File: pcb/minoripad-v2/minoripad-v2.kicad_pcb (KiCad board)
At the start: 2 copper layers, 70 x 50 mm, 42 parts, among them J1 USB_C_Receptacle_USB2.0, SW1 SW_Push, SW2 SW_Push, U1 W25Q16JVSSIQ, U2 SRV05-4, U3 XC6206P332MR, U4 RP2040, Y1 12MHz

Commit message: feat: smaller pcb + case design
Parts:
- moved J1 114.0 mm to (64.1, 27.6), turned to 0 degrees
- moved U2 111.7 mm to (64.1, 36.6)
- moved F1 97.3 mm to (59.8, 35.3), turned to 90 degrees
- moved R3 96.2 mm to (66.6, 33.6), turned to 0 degrees
- moved C7 94.3 mm to (112.8, 60.5)
- moved Y1 94.3 mm to (113.6, 75.4)
- moved C1 94.3 mm to (125.1, 66.3)
- moved C10 94.3 mm to (119.4, 66.3)
- moved C11 94.3 mm to (119.4, 68.3)
- moved C12 94.3 mm to (119.4, 70.2)
- moved C13 94.3 mm to (119.4, 72.2)
- moved C14 94.3 mm to (116.5, 66.3)
- moved C15 94.3 mm to (116.5, 68.3)
- moved C16 94.3 mm to (116.5, 70.2)
- moved C17 94.3 mm to (116.5, 72.2)
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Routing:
- net GND: track 0.00 -> 19.9 mm
- net D-: track 0.00 -> 12.6 mm
- net D+: track 0.00 -> 11.0 mm
- net VBUS: track 0.00 -> 7.80 mm
- net Net-(J1-CC1): track 0.00 -> 1.99 mm
- net Net-(J1-CC2): track 0.00 -> 1.99 mm
- added copper zone on B.Cu, net GND
- added copper zone on F.Cu, net GND

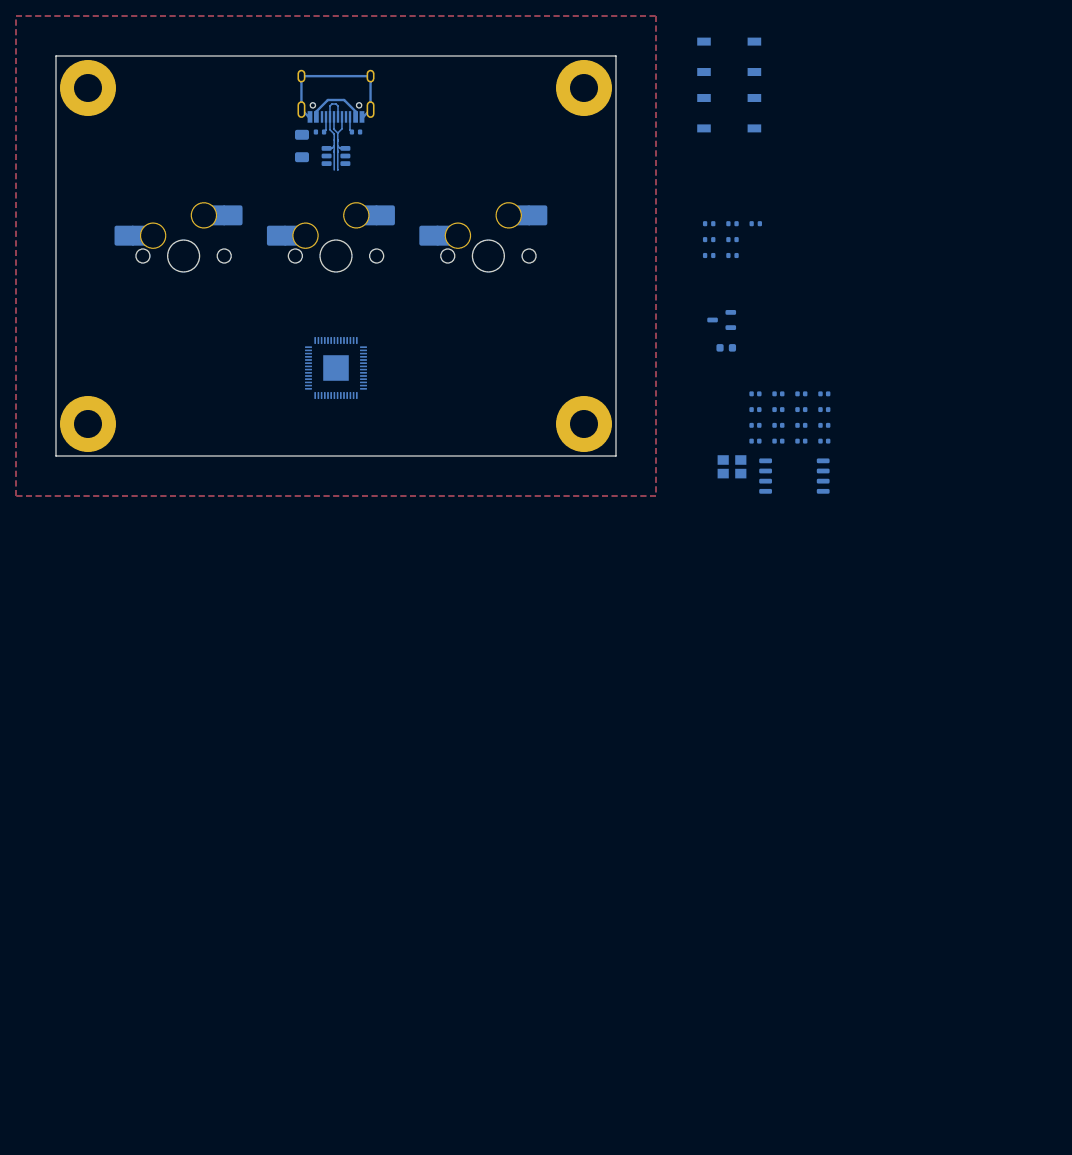
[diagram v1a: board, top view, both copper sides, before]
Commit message: feat: finalise pcb sizing, case cutouts and key positions
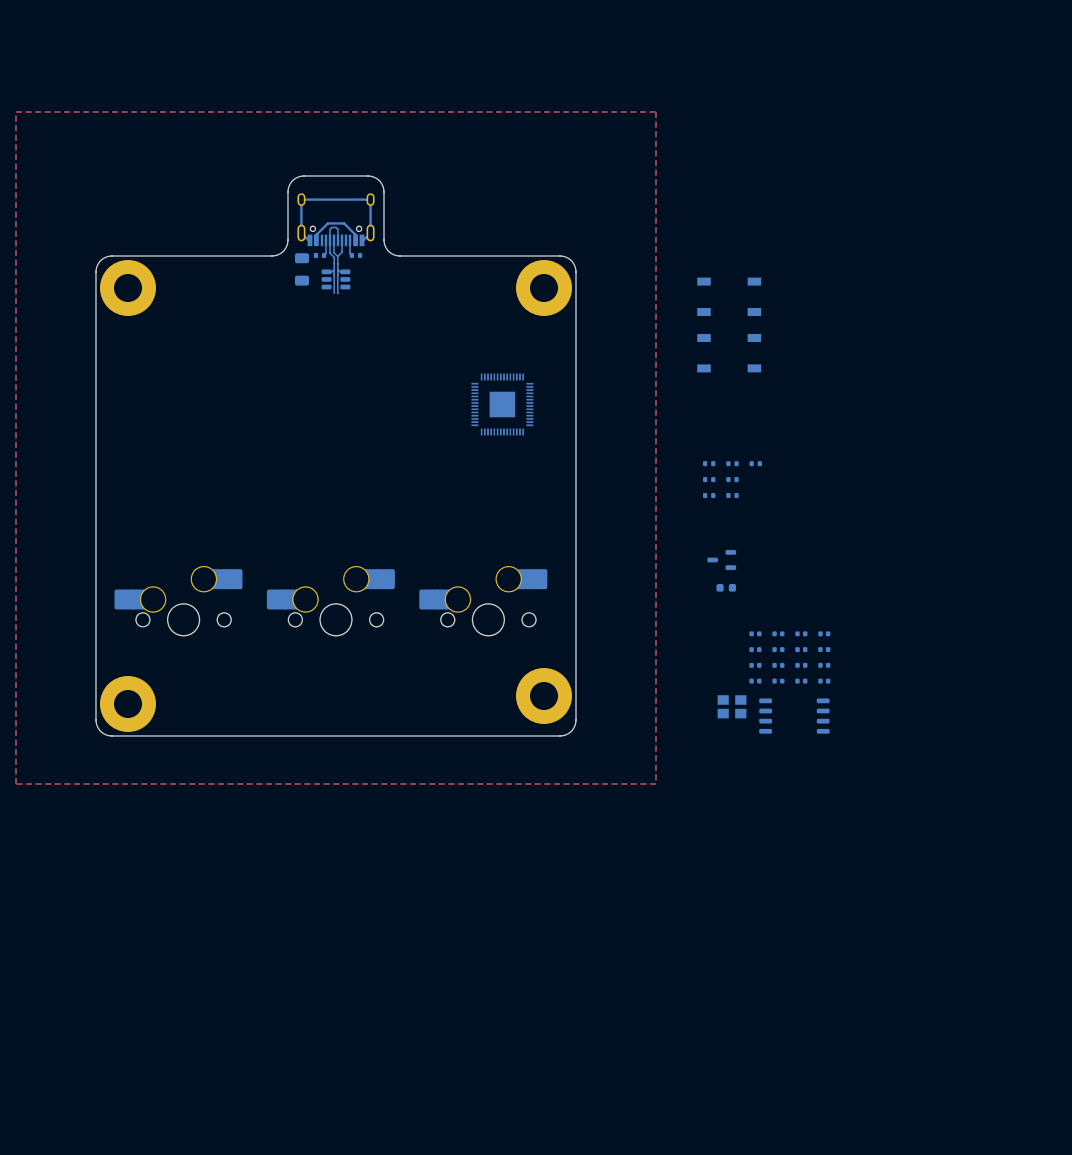
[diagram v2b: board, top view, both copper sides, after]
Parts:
- moved MX1 45.5 mm to (45.0, 94.5)
- moved MX2 45.5 mm to (64.1, 94.5)
- moved MX3 45.5 mm to (83.1, 94.5)
- moved H3 35.4 mm to (38.1, 105.1)
- moved H4 34.4 mm to (90.1, 104.1)
- moved C7 30.0 mm to (112.8, 90.5)
- moved C1 30.0 mm to (125.1, 96.3)
- moved C10 30.0 mm to (119.4, 96.3)
- moved C11 30.0 mm to (119.4, 98.3)
- moved C12 30.0 mm to (119.4, 100.2)
- moved C13 30.0 mm to (119.4, 102.2)
- moved C14 30.0 mm to (116.5, 96.3)
- moved C15 30.0 mm to (116.5, 98.3)
- moved C16 30.0 mm to (116.5, 100.2)
- moved C17 30.0 mm to (116.5, 102.2)
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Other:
- board size 70 x 50 mm -> 60 x 70 mm

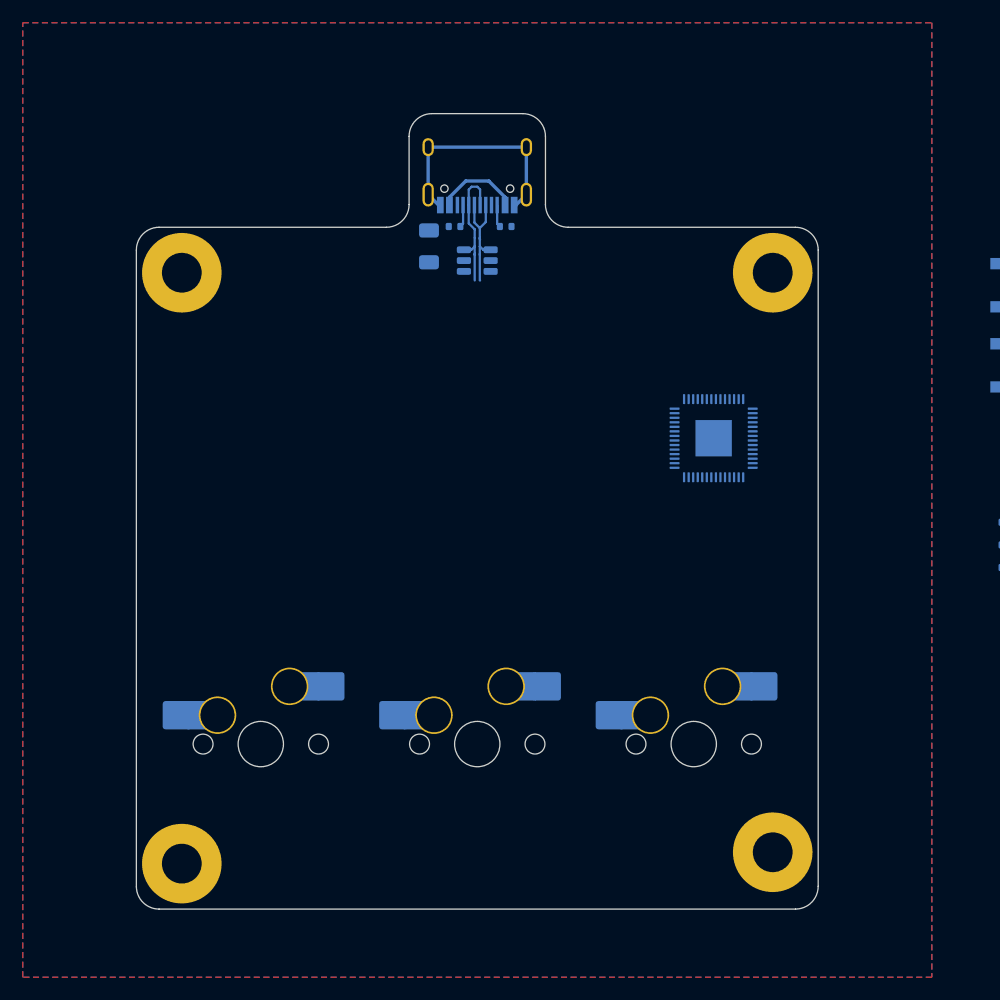
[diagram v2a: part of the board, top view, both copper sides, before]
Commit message: fix: correct usb cutout distance on minoripad
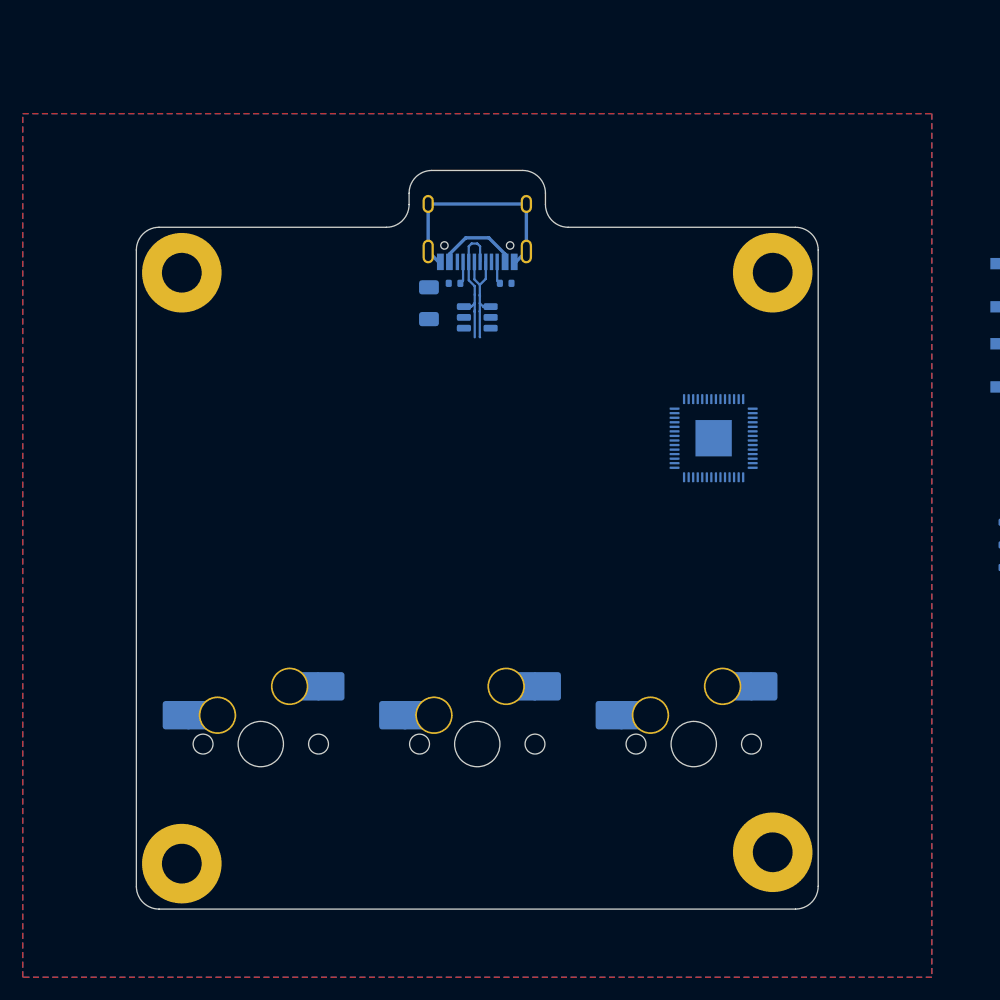
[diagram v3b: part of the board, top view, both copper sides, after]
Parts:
- moved F1 5.00 mm to (59.8, 55.7)
- moved J1 5.00 mm to (64.1, 48.1)
- moved R2 5.00 mm to (62.1, 54.0)
- moved R3 5.00 mm to (66.6, 54.0)
- moved U2 5.00 mm to (64.1, 57.0)
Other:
- board size 60 x 70 mm -> 60 x 65 mm
